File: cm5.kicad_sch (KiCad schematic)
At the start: 35 parts, among them J2 JST_SH_1x3_BM03B-SRSS-TB-LF-SN, J3 CM5_1-100_3mm-stack, J4 CM5_101-200_3mm-stack, J5 JST_SH_1x4_BM04B-SRSS-TB-LF-SN, SW1 SW_TL2243

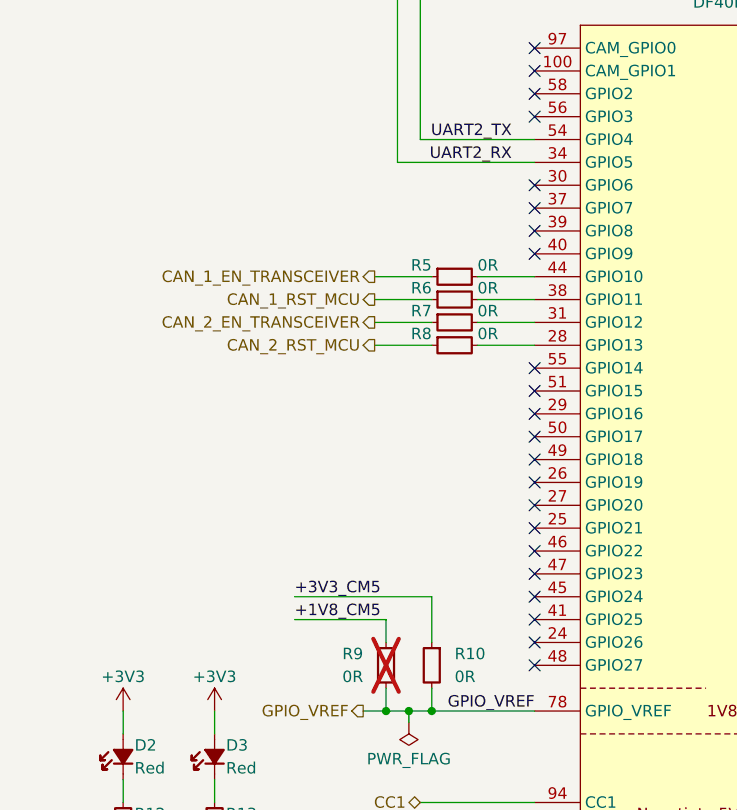
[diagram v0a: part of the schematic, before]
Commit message: [#3] Layout USB to CAN converter and remaining low speed signals
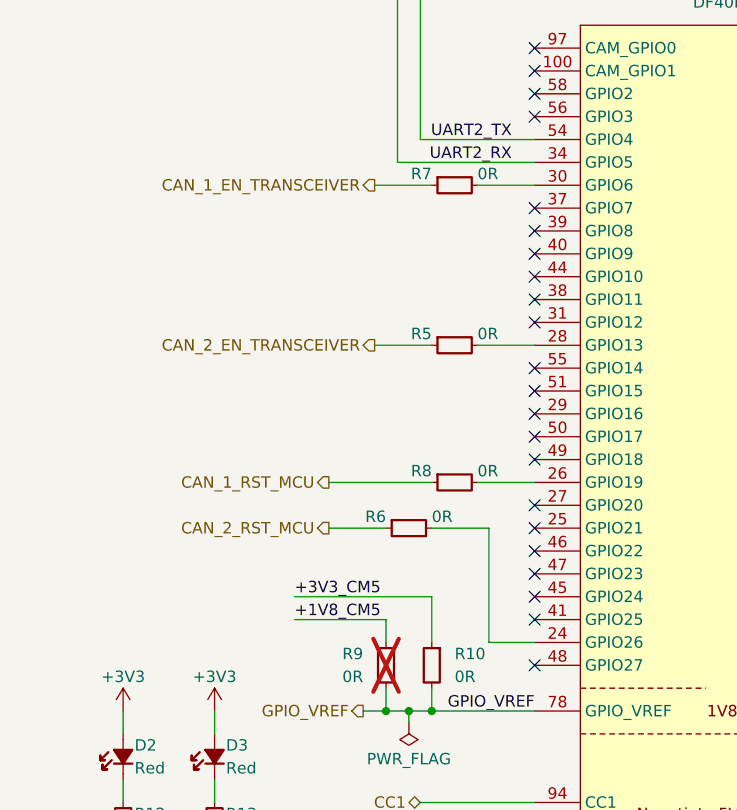
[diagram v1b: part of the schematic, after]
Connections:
- net CAN_1_EN_TRANSCEIVER: now also R7.1; no longer R5.1
- net CAN_1_RST_MCU: now also R8.1; no longer R6.1
- net CAN_2_EN_TRANSCEIVER: now also R5.1; no longer R7.1
- net CAN_2_RST_MCU: now also R6.1; no longer R8.1
- net at R6.2: now also J3.24 (GPIO26); no longer J3.38 (GPIO11)
- net at R8.2: now also J3.26 (GPIO19); no longer J3.28 (GPIO13)
- net at J3.30 (GPIO6): now also R7.2
- net at J3.31 (GPIO12): no longer R7.2
- net at R5.2: now also J3.28 (GPIO13); no longer J3.44 (GPIO10)
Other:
- moved on the sheet: R5, R6, R7, R8
